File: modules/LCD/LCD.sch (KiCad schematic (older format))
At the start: 11 parts, among them J1 Conn_01x10_Male, J2 Conn_01x10_Male

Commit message: LCD shield in work
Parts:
- removed H5, H6, H7, H8: MountingHole, MountingHole:MountingHole_3.2mm_M3, symbol Mechanical:MountingHole
- added RV1: R_POT, Potentiometer_THT:Potentiometer_ACP_CA9-V10_Vertical, symbol Device:R_POT
- DS1: footprint Display:WC1602A -> CommonLibrary:WH1602-2-holes
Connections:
- net GND: now also DS1.1 (VSS), DS1.16 (LED(-)), DS1.5 (R/W), RV1.3
- net VCC: now also DS1.15 (LED(+)), DS1.2 (VDD), RV1.1
- net at DS1.3 (VO): now also RV1.2
- no-connect marks 0 -> 16
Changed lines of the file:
@@
 U 1 1 5E9C831B
 P 2800 2200
-F 0 "DS1" H 2800 1219 50  0000 C CNN
-F 1 "WC1602A" H 2800 1310 50  0000 C CNN
-F 2 "Display:WC1602A" H 2800 1300 50  0001 C CIN
+F 0 "DS1" H 3050 1425 50  0000 C CNN
+F 1 "WC1602A" H 2500 1425 50  0000 C CNN
+F 2 "CommonLibrary:WH1602-2-holes" H 2800 1300 50  0001 C CIN
 F 3 "http://www.wincomlcd.com/pdf/WC1602A-SFYLYHTC06.pdf" H 3500 2200 50  0001 C CNN
 	1    2800 2200
@@
 Wire Wire Line
 	3350 2900 3500 2900
+Text Label 3325 2300 0    50   ~ 0
+D0
+Text Label 3325 2200 0    50   ~ 0
+D1
+Text Label 3325 2100 0    50   ~ 0
+D2
+Text Label 3325 2000 0    50   ~ 0
+D3
+Text Label 3350 2400 0    50   ~ 0
+RS
+Text Label 3375 2900 0    50   ~ 0
+E
 $Comp
-L Mechanical:MountingHole H5
-U 1 1 5E9CFED0
-P 7250 1500
-F 0 "H5" H 7350 1546 50  0000 L CNN
-F 1 "MountingHole" H 7350 1455 50  0000 L CNN
-F 2 "MountingHole:MountingHole_3.2mm_M3" H 7250 1500 50  0001 C CNN
-F 3 "~" H 7250 1500 50  0001 C CNN
-	1    7250 1500
+L power:GND #PWR0103
+U 1 1 5E9CE3ED
+P 2325 2400
+F 0 "#PWR0103" H 2325 2150 50  0001 C CNN
+F 1 "GND" H 2330 2227 50  0000 C CNN
+F 2 "" H 2325 2400 50  0001 C CNN
+F 3 "" H 2325 2400 50  0001 C CNN
+	1    2325 2400
+	-1   0    0    1
+$EndComp
+$Comp
+L power:VCC #PWR0104
+U 1 1 5E9CEA10
+P 2325 2500
+F 0 "#PWR0104" H 2325 2350 50  0001 C CNN
+F 1 "VCC" H 2343 2673 50  0000 C CNN
+F 2 "" H 2325 2500 50  0001 C CNN
+F 3 "" H 2325 2500 50  0001 C CNN
+	1    2325 2500
+	-1   0    0    1
+$EndComp
+Wire Wire Line
+	2325 2400 2400 2400
+Wire Wire Line
+	2325 2500 2400 2500
+$Comp
+L power:VCC #PWR0105
+U 1 1 5E9D01F3
+P 2800 3000
+F 0 "#PWR0105" H 2800 2850 50  0001 C CNN
+F 1 "VCC" H 2818 3173 50  0000 C CNN
+F 2 "" H 2800 3000 50  0001 C CNN
+F 3 "" H 2800 3000 50  0001 C CNN
+	1    2800 3000
+	-1   0    0    1
+$EndComp
+$Comp
+L power:GND #PWR0106
+U 1 1 5E9D0D63
+P 2800 1400
+F 0 "#PWR0106" H 2800 1150 50  0001 C CNN
+F 1 "GND" H 2805 1227 50  0000 C CNN
+F 2 "" H 2800 1400 50  0001 C CNN
+F 3 "" H 2800 1400 50  0001 C CNN
+	1    2800 1400
+	-1   0    0    1
+$EndComp
+$Comp
+L Device:R_POT RV1
+U 1 1 5E9D1EF9
+P 2100 2800
+F 0 "RV1" H 2031 2846 50  0000 R CNN
+F 1 "R_POT" H 2031 2755 50  0000 R CNN
+F 2 "Potentiometer_THT:Potentiometer_ACP_CA9-V10_Vertical" H 2100 2800 50  0001 C CNN
+F 3 "~" H 2100 2800 50  0001 C CNN
+	1    2100 2800
 	1    0    0    -1
 $EndComp
 $Comp
-L Mechanical:MountingHole H6
-U 1 1 5E9CFED6
-P 7250 2000
-F 0 "H6" H 7350 2046 50  0000 L CNN
-F 1 "MountingHole" H 7350 1955 50  0000 L CNN
-F 2 "MountingHole:MountingHole_3.2mm_M3" H 7250 2000 50  0001 C CNN
-F 3 "~" H 7250 2000 50  0001 C CNN
-	1    7250 2000
+L power:GND #PWR0107
+U 1 1 5E9D2907
+P 2100 2950
+F 0 "#PWR0107" H 2100 2700 50  0001 C CNN
+F 1 "GND" H 2105 2777 50  0000 C CNN
+F 2 "" H 2100 2950 50  0001 C CNN
+F 3 "" H 2100 2950 50  0001 C CNN
+	1    2100 2950
 	1    0    0    -1
 $EndComp
 $Comp
-L Mechanical:MountingHole H7
-U 1 1 5E9CFEDC
-P 7250 2500
-F 0 "H7" H 7350 2546 50  0000 L CNN
-F 1 "MountingHole" H 7350 2455 50  0000 L CNN
-F 2 "MountingHole:MountingHole_3.2mm_M3" H 7250 2500 50  0001 C CNN
-F 3 "~" H 7250 2500 50  0001 C CNN
-	1    7250 2500
+L power:VCC #PWR0108
+U 1 1 5E9D2E26
+P 2100 2650
+F 0 "#PWR0108" H 2100 2500 50  0001 C CNN
+F 1 "VCC" H 2117 2823 50  0000 C CNN
+F 2 "" H 2100 2650 50  0001 C CNN
+F 3 "" H 2100 2650 50  0001 C CNN
+	1    2100 2650
 	1    0    0    -1
 $EndComp
+Wire Wire Line
+	2250 2800 2400 2800
 $Comp
-L Mechanical:MountingHole H8
-U 1 1 5E9CFEE2
-P 7250 3000
-F 0 "H8" H 7350 3046 50  0000 L CNN
-F 1 "MountingHole" H 7350 2955 50  0000 L CNN
-F 2 "MountingHole:MountingHole_3.2mm_M3" H 7250 3000 50  0001 C CNN
-F 3 "~" H 7250 3000 50  0001 C CNN
-	1    7250 3000
-	1    0    0    -1
+L power:GND #PWR0109
+U 1 1 5E9D425E
+P 3200 2700
+F 0 "#PWR0109" H 3200 2450 50  0001 C CNN
+F 1 "GND" V 3205 2572 50  0000 R CNN
+F 2 "" H 3200 2700 50  0001 C CNN
+F 3 "" H 3200 2700 50  0001 C CNN
+	1    3200 2700
+	0    -1   -1   0
 $EndComp
+NoConn ~ 1750 2100
+NoConn ~ 1750 2200
+NoConn ~ 1750 2300
+NoConn ~ 1750 2400
+NoConn ~ 1750 2500
+NoConn ~ 1750 2600
+NoConn ~ 1750 2700
+NoConn ~ 1750 2800
+NoConn ~ 3200 1600
+NoConn ~ 3200 1700
+NoConn ~ 3200 1800
+NoConn ~ 3200 1900
+NoConn ~ 3500 2500
+NoConn ~ 3500 2600
+NoConn ~ 3500 2700
+NoConn ~ 3500 2800
 $EndSCHEMATC

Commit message: LCD is ready
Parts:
- RV1: footprint Potentiometer_THT:Potentiometer_ACP_CA9-V10_Vertical -> CommonLibrary:pot-5x5
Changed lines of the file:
@@
 F 0 "RV1" H 2031 2846 50  0000 R CNN
 F 1 "R_POT" H 2031 2755 50  0000 R CNN
-F 2 "Potentiometer_THT:Potentiometer_ACP_CA9-V10_Vertical" H 2100 2800 50  0001 C CNN
+F 2 "CommonLibrary:pot-5x5" H 2100 2800 50  0001 C CNN
 F 3 "~" H 2100 2800 50  0001 C CNN
 	1    2100 2800

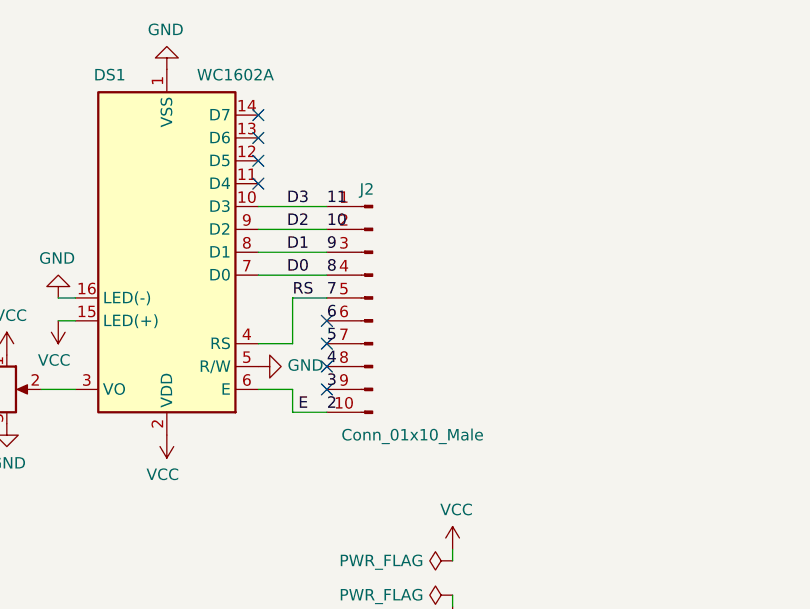
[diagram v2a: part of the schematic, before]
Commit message: Fix LCD pins
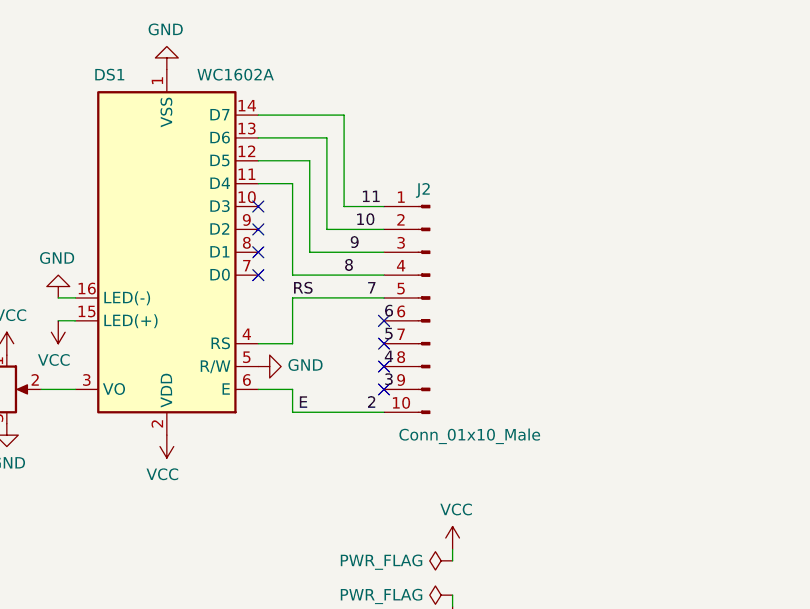
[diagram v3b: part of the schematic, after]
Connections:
- net 10: now also DS1.13 (D6); no longer DS1.9 (D2)
- net 11: now also DS1.14 (D7); no longer DS1.10 (D3)
- net 8: now also DS1.11 (D4); no longer DS1.7 (D0)
- net 9: now also DS1.12 (D5); no longer DS1.8 (D1)
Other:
- moved on the sheet: J2
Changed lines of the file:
@@
 L Connector:Conn_01x10_Male J2
 U 1 1 5E7C1FC2
-P 3700 2400
-F 0 "J2" H 3725 2875 50  0000 C CNN
-F 1 "Conn_01x10_Male" H 3525 1800 50  0000 C CNN
-F 2 "Connector_PinSocket_2.54mm:PinSocket_1x10_P2.54mm_Vertical" H 3700 2400 50  0001 C CNN
-F 3 "~" H 3700 2400 50  0001 C CNN
-	1    3700 2400
+P 3950 2400
+F 0 "J2" H 3975 2875 50  0000 C CNN
+F 1 "Conn_01x10_Male" H 3775 1800 50  0000 C CNN
+F 2 "Connector_PinSocket_2.54mm:PinSocket_1x10_P2.54mm_Vertical" H 3950 2400 50  0001 C CNN
+F 3 "~" H 3950 2400 50  0001 C CNN
+	1    3950 2400
 	-1   0    0    -1
 $EndComp
@@
 Text Label 1750 2800 0    50   ~ 0
 A5
-Text Label 3500 2000 0    50   ~ 0
+Text Label 3650 2000 0    50   ~ 0
 11
-Text Label 3500 2900 0    50   ~ 0
-2
-Text Label 3500 2800 0    50   ~ 0
+Text Label 3750 2800 0    50   ~ 0
 3
-Text Label 3500 2700 0    50   ~ 0
+Text Label 3750 2700 0    50   ~ 0
 4
-Text Label 3500 2600 0    50   ~ 0
+Text Label 3750 2600 0    50   ~ 0
 5
-Text Label 3500 2500 0    50   ~ 0
+Text Label 3750 2500 0    50   ~ 0
 6
-Text Label 3500 2400 0    50   ~ 0
+Text Label 3675 2400 0    50   ~ 0
 7
-Text Label 3500 2300 0    50   ~ 0
+Text Label 3575 2300 0    50   ~ 0
 8
-Text Label 3500 2200 0    50   ~ 0
+Text Label 3600 2200 0    50   ~ 0
 9
-Text Label 3500 2100 0    50   ~ 0
+Text Label 3625 2100 0    50   ~ 0
 10
 $Comp
@@
 $EndComp
 Wire Wire Line
-	3200 2000 3500 2000
-Wire Wire Line
-	3200 2100 3500 2100
-Wire Wire Line
-	3200 2200 3500 2200
-Wire Wire Line
-	3200 2300 3500 2300
-Wire Wire Line
 	3200 2600 3350 2600
 Wire Wire Line
 	3350 2600 3350 2400
 Wire Wire Line
-	3350 2400 3500 2400
-Wire Wire Line
 	3200 2800 3350 2800
 Wire Wire Line
 	3350 2800 3350 2900
-Wire Wire Line
-	3350 2900 3500 2900
-Text Label 3325 2300 0    50   ~ 0
-D0
-Text Label 3325 2200 0    50   ~ 0
-D1
-Text Label 3325 2100 0    50   ~ 0
-D2
-Text Label 3325 2000 0    50   ~ 0
-D3
 Text Label 3350 2400 0    50   ~ 0
 RS
@@
 NoConn ~ 1750 2700
 NoConn ~ 1750 2800
-NoConn ~ 3200 1600
-NoConn ~ 3200 1700
-NoConn ~ 3200 1800
-NoConn ~ 3200 1900
-NoConn ~ 3500 2500
-NoConn ~ 3500 2600
-NoConn ~ 3500 2700
-NoConn ~ 3500 2800
+NoConn ~ 3200 2000
+NoConn ~ 3200 2100
+NoConn ~ 3200 2200
+NoConn ~ 3200 2300
+Wire Wire Line
+	3350 2400 3750 2400
+Wire Wire Line
+	3200 1900 3350 1900
+Wire Wire Line
+	3350 1900 3350 2300
+Wire Wire Line
+	3350 2300 3750 2300
+Wire Wire Line
+	3200 1800 3425 1800
+Wire Wire Line
+	3425 1800 3425 2200
+Wire Wire Line
+	3425 2200 3750 2200
+Wire Wire Line
+	3200 1700 3500 1700
+Wire Wire Line
+	3500 1700 3500 2100
+Wire Wire Line
+	3500 2100 3750 2100
+Wire Wire Line
+	3200 1600 3575 1600
+Wire Wire Line
+	3575 1600 3575 2000
+Wire Wire Line
+	3575 2000 3750 2000
+NoConn ~ 3750 2500
+NoConn ~ 3750 2600
+NoConn ~ 3750 2700
+NoConn ~ 3750 2800
+Wire Wire Line
+	3350 2900 3750 2900
+Text Label 3675 2900 0    50   ~ 0
+2
 $EndSCHEMATC

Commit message: My LCD does not have LED resistor :( Add silk etc
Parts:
- added R1: 20, Resistor_SMD:R_0805_2012Metric_Pad1.15x1.40mm_HandSolder, symbol Device:R
- DS1: value WC1602A -> WH1602B
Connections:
- net GND: now also R1.2; no longer DS1.16 (LED(-))
- new net: DS1.16 (LED(-)), R1.1
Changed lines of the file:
@@
 P 2800 2200
 F 0 "DS1" H 3050 1425 50  0000 C CNN
-F 1 "WC1602A" H 2500 1425 50  0000 C CNN
+F 1 "WH1602B" H 2500 1425 50  0000 C CNN
 F 2 "CommonLibrary:WH1602-2-holes" H 2800 1300 50  0001 C CIN
 F 3 "http://www.wincomlcd.com/pdf/WC1602A-SFYLYHTC06.pdf" H 3500 2200 50  0001 C CNN
@@
 L power:GND #PWR0103
 U 1 1 5E9CE3ED
-P 2325 2400
-F 0 "#PWR0103" H 2325 2150 50  0001 C CNN
-F 1 "GND" H 2330 2227 50  0000 C CNN
-F 2 "" H 2325 2400 50  0001 C CNN
-F 3 "" H 2325 2400 50  0001 C CNN
-	1    2325 2400
+P 2325 2100
+F 0 "#PWR0103" H 2325 1850 50  0001 C CNN
+F 1 "GND" H 2330 1927 50  0000 C CNN
+F 2 "" H 2325 2100 50  0001 C CNN
+F 3 "" H 2325 2100 50  0001 C CNN
+	1    2325 2100
 	-1   0    0    1
 $EndComp
@@
 Text Label 3675 2900 0    50   ~ 0
 2
+$Comp
+L Device:R R1
+U 1 1 5EAB4E35
+P 2325 2250
+F 0 "R1" H 2256 2204 50  0000 R CNN
+F 1 "20" H 2256 2295 50  0000 R CNN
+F 2 "Resistor_SMD:R_0805_2012Metric_Pad1.15x1.40mm_HandSolder" V 2255 2250 50  0001 C CNN
+F 3 "~" H 2325 2250 50  0001 C CNN
+	1    2325 2250
+	1    0    0    1
+$EndComp
 $EndSCHEMATC

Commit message: LED polishing
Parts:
- RV1: footprint CommonLibrary:pot-5x5 -> Potentiometer_THT:Potentiometer_ACP_CA6-H2,5_Horizontal
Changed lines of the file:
@@
 F 0 "RV1" H 2031 2846 50  0000 R CNN
 F 1 "R_POT" H 2031 2755 50  0000 R CNN
-F 2 "CommonLibrary:pot-5x5" H 2100 2800 50  0001 C CNN
+F 2 "Potentiometer_THT:Potentiometer_ACP_CA6-H2,5_Horizontal" H 2100 2800 50  0001 C CNN
 F 3 "~" H 2100 2800 50  0001 C CNN
 	1    2100 2800

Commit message: LCD polishing
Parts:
- J1, J2: footprint Connector_PinSocket_2.54mm:PinSocket_1x10_P2.54mm_Vertical -> Connector_PinHeader_2.54mm:PinHeader_1x10_P2.54mm_Vertical
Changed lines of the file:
@@
 F 0 "J1" H 1550 2900 50  0000 C CNN
 F 1 "Conn_01x10_Male" H 1400 1800 50  0000 C CNN
-F 2 "Connector_PinSocket_2.54mm:PinSocket_1x10_P2.54mm_Vertical" H 1550 2400 50  0001 C CNN
+F 2 "Connector_PinHeader_2.54mm:PinHeader_1x10_P2.54mm_Vertical" H 1550 2400 50  0001 C CNN
 F 3 "~" H 1550 2400 50  0001 C CNN
 	1    1550 2400
@@
 F 0 "J2" H 3975 2875 50  0000 C CNN
 F 1 "Conn_01x10_Male" H 3775 1800 50  0000 C CNN
-F 2 "Connector_PinSocket_2.54mm:PinSocket_1x10_P2.54mm_Vertical" H 3950 2400 50  0001 C CNN
+F 2 "Connector_PinHeader_2.54mm:PinHeader_1x10_P2.54mm_Vertical" H 3950 2400 50  0001 C CNN
 F 3 "~" H 3950 2400 50  0001 C CNN
 	1    3950 2400

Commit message: Add 74LS139 for kbd
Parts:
- added J3: Conn_01x04_Female, Connector_PinSocket_2.54mm:PinSocket_1x04_P2.54mm_Vertical, symbol Connector:Conn_01x04_Female
- added J4: Conn_01x02_Female, Connector_PinSocket_2.54mm:PinSocket_1x02_P2.54mm_Vertical, symbol Connector:Conn_01x02_Female
- added R2: 10k, Resistor_SMD:R_0805_2012Metric_Pad1.15x1.40mm_HandSolder, symbol Device:R
- added U1: 74LS139, Package_SO:SOIC-16_3.9x9.9mm_P1.27mm, symbol 74xx_IEEE:74LS139
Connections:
- net 12: now also U1.2 (A)
- net 13: now also U1.3 (B)
- net 4: now also J4.1 (Pin_1)
- net A3: now also J4.2 (Pin_2)
- net GND: now also U1.1 (~EN), U1.8 (GND), U1.8 (GND)
- net VCC: now also R2.2, U1.16 (VCC), U1.16 (VCC)
- new net: J3.1 (Pin_1), U1.4 (~Q0)
- new net: J3.2 (Pin_2), U1.5 (~Q1)
- new net: J3.3 (Pin_3), U1.6 (~Q2)
- new net: J3.4 (Pin_4), U1.7 (~Q3)
- new net: R2.1, U1.13 (B), U1.14 (A), U1.15 (~EN)
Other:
- note added: "To Kbd"
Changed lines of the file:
@@
 L power:GND #PWR0101
 U 1 1 5E4E1E07
-P 4050 3750
-F 0 "#PWR0101" H 4050 3500 50  0001 C CNN
-F 1 "GND" H 4055 3577 50  0000 C CNN
-F 2 "" H 4050 3750 50  0001 C CNN
-F 3 "" H 4050 3750 50  0001 C CNN
-	1    4050 3750
+P 5500 2225
+F 0 "#PWR0101" H 5500 1975 50  0001 C CNN
+F 1 "GND" H 5505 2052 50  0000 C CNN
+F 2 "" H 5500 2225 50  0001 C CNN
+F 3 "" H 5500 2225 50  0001 C CNN
+	1    5500 2225
 	1    0    0    -1
 $EndComp
@@
 L power:VCC #PWR0102
 U 1 1 5E4E268A
-P 4050 3500
-F 0 "#PWR0102" H 4050 3350 50  0001 C CNN
-F 1 "VCC" H 4067 3673 50  0000 C CNN
-F 2 "" H 4050 3500 50  0001 C CNN
-F 3 "" H 4050 3500 50  0001 C CNN
-	1    4050 3500
-	1    0    0    -1
-$EndComp
-Wire Wire Line
-	4050 3500 4050 3550
-Wire Wire Line
-	4050 3700 4050 3750
+P 5500 1975
+F 0 "#PWR0102" H 5500 1825 50  0001 C CNN
+F 1 "VCC" H 5517 2148 50  0000 C CNN
+F 2 "" H 5500 1975 50  0001 C CNN
+F 3 "" H 5500 1975 50  0001 C CNN
+	1    5500 1975
+	1    0    0    -1
+$EndComp
+Wire Wire Line
+	5500 1975 5500 2025
+Wire Wire Line
+	5500 2175 5500 2225
 $Comp
 L power:PWR_FLAG #FLG0101
 U 1 1 5E4E36FF
-P 4050 3550
-F 0 "#FLG0101" H 4050 3625 50  0001 C CNN
-F 1 "PWR_FLAG" V 4050 3677 50  0000 L CNN
-F 2 "" H 4050 3550 50  0001 C CNN
-F 3 "~" H 4050 3550 50  0001 C CNN
-	1    4050 3550
+P 5500 2025
+F 0 "#FLG0101" H 5500 2100 50  0001 C CNN
+F 1 "PWR_FLAG" V 5500 2152 50  0000 L CNN
+F 2 "" H 5500 2025 50  0001 C CNN
+F 3 "~" H 5500 2025 50  0001 C CNN
+	1    5500 2025
 	0    -1   -1   0
 $EndComp
@@
 L power:PWR_FLAG #FLG0102
 U 1 1 5E4E3D09
-P 4050 3700
-F 0 "#FLG0102" H 4050 3775 50  0001 C CNN
-F 1 "PWR_FLAG" V 4050 3827 50  0000 L CNN
-F 2 "" H 4050 3700 50  0001 C CNN
-F 3 "~" H 4050 3700 50  0001 C CNN
-	1    4050 3700
+P 5500 2175
+F 0 "#FLG0102" H 5500 2250 50  0001 C CNN
+F 1 "PWR_FLAG" V 5500 2302 50  0000 L CNN
+F 2 "" H 5500 2175 50  0001 C CNN
+F 3 "~" H 5500 2175 50  0001 C CNN
+	1    5500 2175
 	0    -1   -1   0
 $EndComp
@@
 	0    -1   -1   0
 $EndComp
-NoConn ~ 1750 2100
-NoConn ~ 1750 2200
 NoConn ~ 1750 2300
 NoConn ~ 1750 2400
 NoConn ~ 1750 2500
-NoConn ~ 1750 2600
 NoConn ~ 1750 2700
 NoConn ~ 1750 2800
@@
 NoConn ~ 3750 2500
 NoConn ~ 3750 2600
-NoConn ~ 3750 2700
 NoConn ~ 3750 2800
 Wire Wire Line
@@
 	1    0    0    1
 $EndComp
+$Comp
+L 74xx_IEEE:74LS139 U1
+U 1 1 5FC2E042
+P 2450 3850
+F 0 "U1" H 2450 4466 50  0000 C CNN
+F 1 "74LS139" H 2450 4375 50  0000 C CNN
+F 2 "Package_SO:SOIC-16_3.9x9.9mm_P1.27mm" H 2450 3850 50  0001 C CNN
+F 3 "http://www.ti.com/lit/ds/symlink/sn74ls139a.pdf" H 2450 3850 50  0001 C CNN
+	1    2450 3850
+	1    0    0    -1
+$EndComp
+$Comp
+L 74xx_IEEE:74LS139 U1
+U 2 1 5FC2EFFA
+P 2450 4975
+F 0 "U1" H 2450 5591 50  0000 C CNN
+F 1 "74LS139" H 2450 5500 50  0000 C CNN
+F 2 "Package_SO:SOIC-16_3.9x9.9mm_P1.27mm" H 2450 4975 50  0001 C CNN
+F 3 "http://www.ti.com/lit/ds/symlink/sn74ls139a.pdf" H 2450 4975 50  0001 C CNN
+	2    2450 4975
+	1    0    0    -1
+$EndComp
+Text Label 1900 3600 0    50   ~ 0
+12
+Text Label 1900 3750 0    50   ~ 0
+13
+$Comp
+L power:GND #PWR02
+U 1 1 5FC31897
+P 1900 4100
+F 0 "#PWR02" H 1900 3850 50  0001 C CNN
+F 1 "GND" H 1905 3927 50  0000 C CNN
+F 2 "" H 1900 4100 50  0001 C CNN
+F 3 "" H 1900 4100 50  0001 C CNN
+	1    1900 4100
+	1    0    0    -1
+$EndComp
+$Comp
+L power:VCC #PWR01
+U 1 1 5FC32D2F
+P 1600 4725
+F 0 "#PWR01" H 1600 4575 50  0001 C CNN
+F 1 "VCC" V 1615 4852 50  0000 L CNN
+F 2 "" H 1600 4725 50  0001 C CNN
+F 3 "" H 1600 4725 50  0001 C CNN
+	1    1600 4725
+	0    -1   -1   0
+$EndComp
+$Comp
+L Device:R R2
+U 1 1 5FC323B0
+P 1750 4725
+F 0 "R2" V 1675 4725 50  0000 C CNN
+F 1 "10k" V 1750 4725 50  0000 C CNN
+F 2 "Resistor_SMD:R_0805_2012Metric_Pad1.15x1.40mm_HandSolder" V 1680 4725 50  0001 C CNN
+F 3 "~" H 1750 4725 50  0001 C CNN
+	1    1750 4725
+	0    1    1    0
+$EndComp
+Wire Wire Line
+	1900 5225 1900 4875
+Wire Wire Line
+	1900 4725 1900 4875
+Connection ~ 1900 4725
+Connection ~ 1900 4875
+NoConn ~ 3000 4725
+NoConn ~ 3000 4875
+NoConn ~ 3000 5075
+NoConn ~ 3000 5225
+$Comp
+L Connector:Conn_01x04_Female J3
+U 1 1 5FC38C89
+P 3450 3700
+F 0 "J3" H 3375 3925 50  0000 L CNN
+F 1 "Conn_01x04_Female" H 3125 3400 50  0000 L CNN
+F 2 "Connector_PinSocket_2.54mm:PinSocket_1x04_P2.54mm_Vertical" H 3450 3700 50  0001 C CNN
+F 3 "~" H 3450 3700 50  0001 C CNN
+	1    3450 3700
+	1    0    0    -1
+$EndComp
+Wire Wire Line
+	3000 3600 3250 3600
+Wire Wire Line
+	3000 3750 3000 3700
+Wire Wire Line
+	3000 3700 3250 3700
+Wire Wire Line
+	3000 3950 3050 3950
+Wire Wire Line
+	3050 3950 3050 3800
+Wire Wire Line
+	3050 3800 3250 3800
+Wire Wire Line
+	3000 4100 3100 4100
+Wire Wire Line
+	3100 4100 3100 3900
+Wire Wire Line
+	3100 3900 3250 3900
+Text Notes 3575 3775 0    50   ~ 0
+To Kbd
+$Comp
+L Connector:Conn_01x02_Female J4
+U 1 1 5FC3BBE8
+P 4025 3700
+F 0 "J4" H 3975 3800 50  0000 L CNN
+F 1 "Conn_01x02_Female" H 3300 3475 50  0000 L CNN
+F 2 "Connector_PinSocket_2.54mm:PinSocket_1x02_P2.54mm_Vertical" H 4025 3700 50  0001 C CNN
+F 3 "~" H 4025 3700 50  0001 C CNN
+	1    4025 3700
+	-1   0    0    -1
+$EndComp
+Text Label 4225 3700 0    50   ~ 0
+4
+Text Label 4225 3800 0    50   ~ 0
+A3
 $EndSCHEMATC
